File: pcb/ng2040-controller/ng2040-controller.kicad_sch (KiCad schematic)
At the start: 12 parts, among them J1 A, J2 B, J3 C, J4 D, J5 START, J6 SELECT, J7 JOY, J8 BATTERY, SW1 SW_DIP_x02, U1 RP2040-Zero, U2 NRF24L01_Breakout

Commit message: controller board
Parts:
- SW1: value SW_DIP_x02 -> OPTS
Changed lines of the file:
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@@
 			)
 		)
-		(property "Value" "SW_DIP_x02"
+		(property "Value" "OPTS"
 			(at 113.03 22.86 0)
 			(effects

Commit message: NG2040 controller board
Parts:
- U2: value NRF24L01_Breakout -> NRF24L01
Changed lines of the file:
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@@
 			)
 		)
-		(property "Value" "NRF24L01_Breakout"
+		(property "Value" "NRF24L01"
 			(at 176.53 66.0399 0)
 			(effects

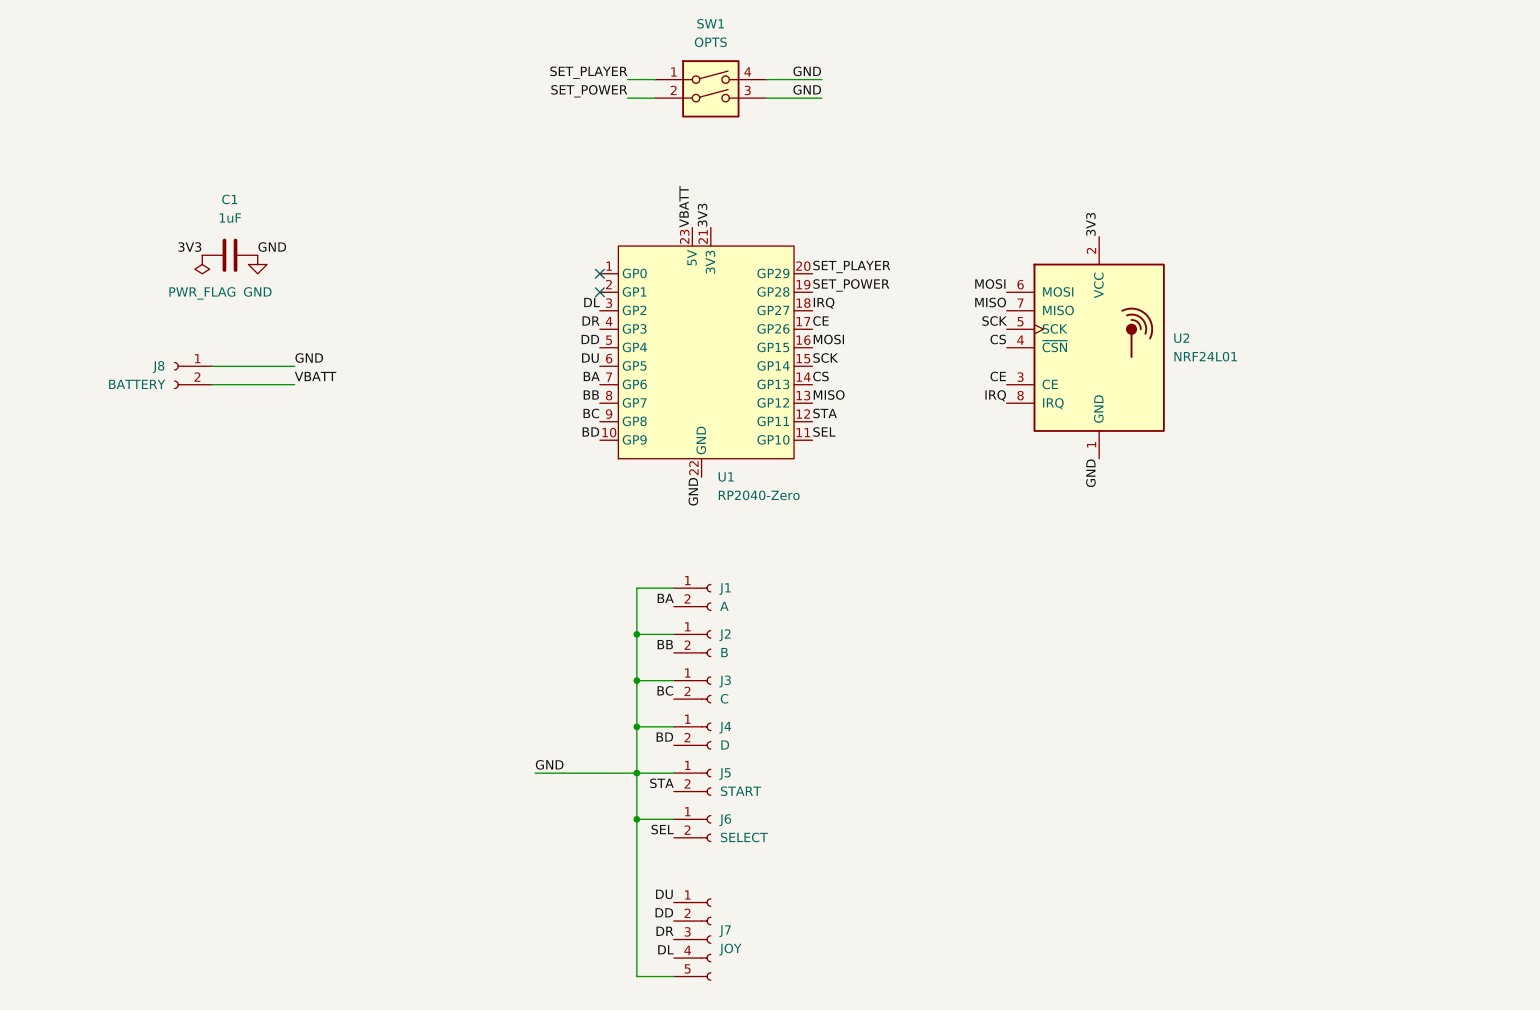
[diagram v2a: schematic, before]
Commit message: Reworking controller board to put pico on back for LED to shine through
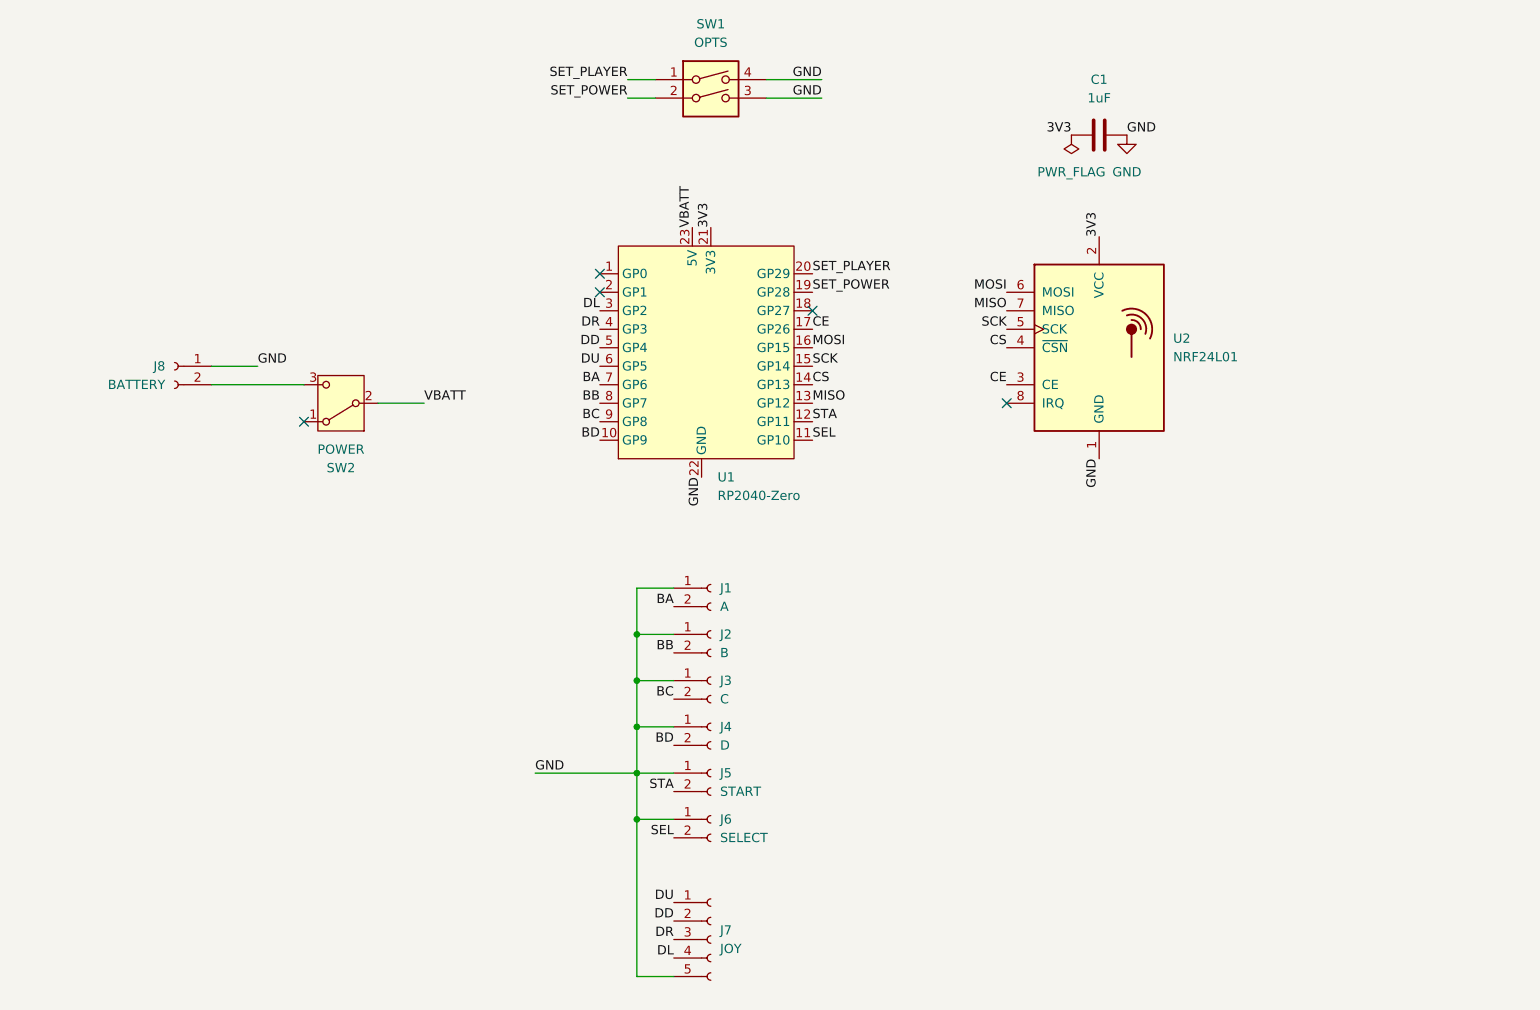
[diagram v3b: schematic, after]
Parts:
- added SW2: POWER, REB_Switch:REB_SlideSwitch_3pin, symbol Switch:SW_SPDT
- SW1: footprint Button_Switch_THT:SW_DIP_SPSTx02_Slide_9.78x7.26mm_W7.62mm_P2.54mm -> Button_Switch_SMD:SW_DIP_SPSTx02_Slide_6.7x6.64mm_W8.61mm_P2.54mm_LowProfile
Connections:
- net VBATT: now also SW2.2 (B); no longer J8.2 (Pin_2)
- net IRQ: no longer names the net of U2.8 (IRQ)
- net IRQ: no longer U1.18 (GP27)
- new net: J8.2 (Pin_2), SW2.3 (C)
- no-connect marks 2 -> 5
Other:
- moved on the sheet: C1
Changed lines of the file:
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@@
+	)
+	(no_connect
+		(at 153.67 72.39)
+	)
+	(no_connect
+		(at 57.15 74.93)
 	)
 	(no_connect
@@
 	)
 	(no_connect
+		(at 127 59.69)
+	)
+	(no_connect
 		(at 97.79 57.15)
 	)
@@
 	(wire
 		(pts
+			(xy 73.66 72.39) (xy 67.31 72.39)
+		)
+		(stroke
+			(width 0)
+			(type default)
+		)
+	)
+	(wire
+		(pts
 			(xy 102.87 97.79) (xy 102.87 104.14)
 		)
@@
 	(wire
 		(pts
-			(xy 55.88 67.31) (xy 44.45 67.31)
+			(xy 50.8 67.31) (xy 44.45 67.31)
 		)
 		(stroke
@@
 	(wire
 		(pts
-			(xy 55.88 69.85) (xy 44.45 69.85)
+			(xy 57.15 69.85) (xy 44.45 69.85)
 		)
 		(stroke
@@
 		)
 	)
-	(label "VBATT"
-		(at 55.88 69.85 0)
-		(fields_autoplaced yes)
-		(effects
-			(font
-				(size 1.27 1.27)
-			)
-			(justify left bottom)
-		)
-	)
 	(label "DL"
 		(at 97.79 59.69 180)
@@
 	)
 	(label "GND"
-		(at 55.88 67.31 0)
+		(at 50.8 67.31 0)
 		(fields_autoplaced yes)
 		(effects
@@
 		)
 	)
-	(label "IRQ"
-		(at 153.67 72.39 180)
-		(fields_autoplaced yes)
-		(effects
-			(font
-				(size 1.27 1.27)
-			)
-			(justify right bottom)
-		)
-	)
 	(label "3V3"
 		(at 166.37 49.53 90)
@@
 	)
 	(label "3V3"
-		(at 43.18 52.07 180)
+		(at 162.56 35.56 180)
 		(fields_autoplaced yes)
 		(effects
@@
 	)
 	(label "GND"
-		(at 50.8 52.07 0)
+		(at 170.18 35.56 0)
 		(fields_autoplaced yes)
 		(effects
@@
 		)
 	)
+	(label "VBATT"
+		(at 73.66 72.39 0)
+		(fields_autoplaced yes)
+		(effects
+			(font
+				(size 1.27 1.27)
+			)
+			(justify left bottom)
+		)
+	)
 	(label "MOSI"
 		(at 153.67 57.15 180)
@@
 			)
 			(justify right bottom)
-		)
-	)
-	(label "IRQ"
-		(at 127 59.69 0)
-		(fields_autoplaced yes)
-		(effects
-			(font
-				(size 1.27 1.27)
-			)
-			(justify left bottom)
 		)
 	)
@@
 				(path "/e91880d7-e1f1-43ba-b9bf-5f0fc90655d2"
 					(reference "J7")
+					(unit 1)
+				)
+			)
+		)
+	)
+	(symbol
+		(lib_id "Switch:SW_SPDT")
+		(at 62.23 72.39 180)
+		(unit 1)
+		(exclude_from_sim no)
+		(in_bom yes)
+		(on_board yes)
+		(dnp no)
+		(property "Reference" "SW2"
+			(at 62.23 81.28 0)
+			(effects
+				(font
+					(size 1.27 1.27)
+				)
+			)
+		)
+		(property "Value" "POWER"
+			(at 62.23 78.74 0)
+			(effects
+				(font
+					(size 1.27 1.27)
+				)
+			)
+		)
+		(property "Footprint" "REB_Switch:REB_SlideSwitch_3pin"
+			(at 62.23 72.39 0)
+			(effects
+				(font
+					(size 1.27 1.27)
+				)
+				(hide yes)
+			)
+		)
+		(property "Datasheet" "~"
+			(at 62.23 64.77 0)
+			(effects
+				(font
+					(size 1.27 1.27)
+				)
+				(hide yes)
+			)
+		)
+		(property "Description" "Switch, single pole double throw"
+			(at 62.23 72.39 0)
+			(effects
+				(font
+					(size 1.27 1.27)
+				)
+				(hide yes)
+			)
+		)
+		(property "Notes" ""
+			(at 62.23 72.39 0)
+			(effects
+				(font
+					(size 1.27 1.27)
+				)
+			)
+		)
+		(pin "2"
+		)
+		(pin "3"
+		)
+		(pin "1"
+		)
+		(instances
+			(project "ng2040-controller"
+				(path "/e91880d7-e1f1-43ba-b9bf-5f0fc90655d2"
+					(reference "SW2")
 					(unit 1)
 				)
@@
 			)
 		)
-		(property "Footprint" "Button_Switch_THT:SW_DIP_SPSTx02_Slide_9.78x7.26mm_W7.62mm_P2.54mm"
+		(property "Footprint" "Button_Switch_SMD:SW_DIP_SPSTx02_Slide_6.7x6.64mm_W8.61mm_P2.54mm_LowProfile"
 			(at 113.03 30.48 0)
 			(effects
@@
 	(symbol
 		(lib_id "power:PWR_FLAG")
-		(at 43.18 52.07 180)
+		(at 162.56 35.56 180)
 		(unit 1)
 		(exclude_from_sim no)
@@
 		(fields_autoplaced yes)
 		(property "Reference" "#FLG01"
-			(at 43.18 53.975 0)
+			(at 162.56 37.465 0)
 			(effects
 				(font
@@
 		)
 		(property "Value" "PWR_FLAG"
-			(at 43.18 57.15 0)
+			(at 162.56 40.64 0)
 			(effects
 				(font
@@
 		)
 		(property "Footprint" ""
-			(at 43.18 52.07 0)
+			(at 162.56 35.56 0)
 			(effects
 				(font
@@
 		)
 		(property "Datasheet" "~"
-			(at 43.18 52.07 0)
+			(at 162.56 35.56 0)
 			(effects
 				(font
@@
 		)
 		(property "Description" ""
-			(at 43.18 52.07 0)
+			(at 162.56 35.56 0)
 			(effects
 				(font
@@
 	(symbol
 		(lib_id "power:GND")
-		(at 50.8 52.07 0)
+		(at 170.18 35.56 0)
 		(unit 1)
 		(exclude_from_sim no)
@@
 		(fields_autoplaced yes)
 		(property "Reference" "#PWR01"
-			(at 50.8 58.42 0)
+			(at 170.18 41.91 0)
 			(effects
 				(font
@@
 		)
 		(property "Value" "GND"
-			(at 50.8 57.15 0)
+			(at 170.18 40.64 0)
 			(effects
 				(font
@@
 		)
 		(property "Footprint" ""
-			(at 50.8 52.07 0)
+			(at 170.18 35.56 0)
 			(effects
 				(font
@@
 		)
 		(property "Datasheet" ""
-			(at 50.8 52.07 0)
+			(at 170.18 35.56 0)
 			(effects
 				(font
@@
 		)
 		(property "Description" ""
-			(at 50.8 52.07 0)
+			(at 170.18 35.56 0)
 			(effects
 				(font
@@
 	(symbol
 		(lib_id "Device:C")
-		(at 46.99 52.07 90)
+		(at 166.37 35.56 90)
 		(unit 1)
 		(exclude_from_sim no)
@@
 		(fields_autoplaced yes)
 		(property "Reference" "C1"
-			(at 46.99 44.45 90)
+			(at 166.37 27.94 90)
 			(effects
 				(font
@@
 		)
 		(property "Value" "1uF"
-			(at 46.99 46.99 90)
+			(at 166.37 30.48 90)
 			(effects
 				(font
@@
 		)
 		(property "Footprint" "Capacitor_SMD:C_0805_2012Metric_Pad1.18x1.45mm_HandSolder"
-			(at 50.8 51.1048 0)
+			(at 170.18 34.5948 0)
 			(effects
 				(font
@@
 		)
 		(property "Datasheet" "~"
-			(at 46.99 52.07 0)
+			(at 166.37 35.56 0)
 			(effects
 				(font
@@
 		)
 		(property "Description" ""
-			(at 46.99 52.07 0)
-			(effects
-				(font
+			(at 166.37 35.56 0)
+			(effects
+				(font

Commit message: WIP changing controller into a narrower one breaking away NRF
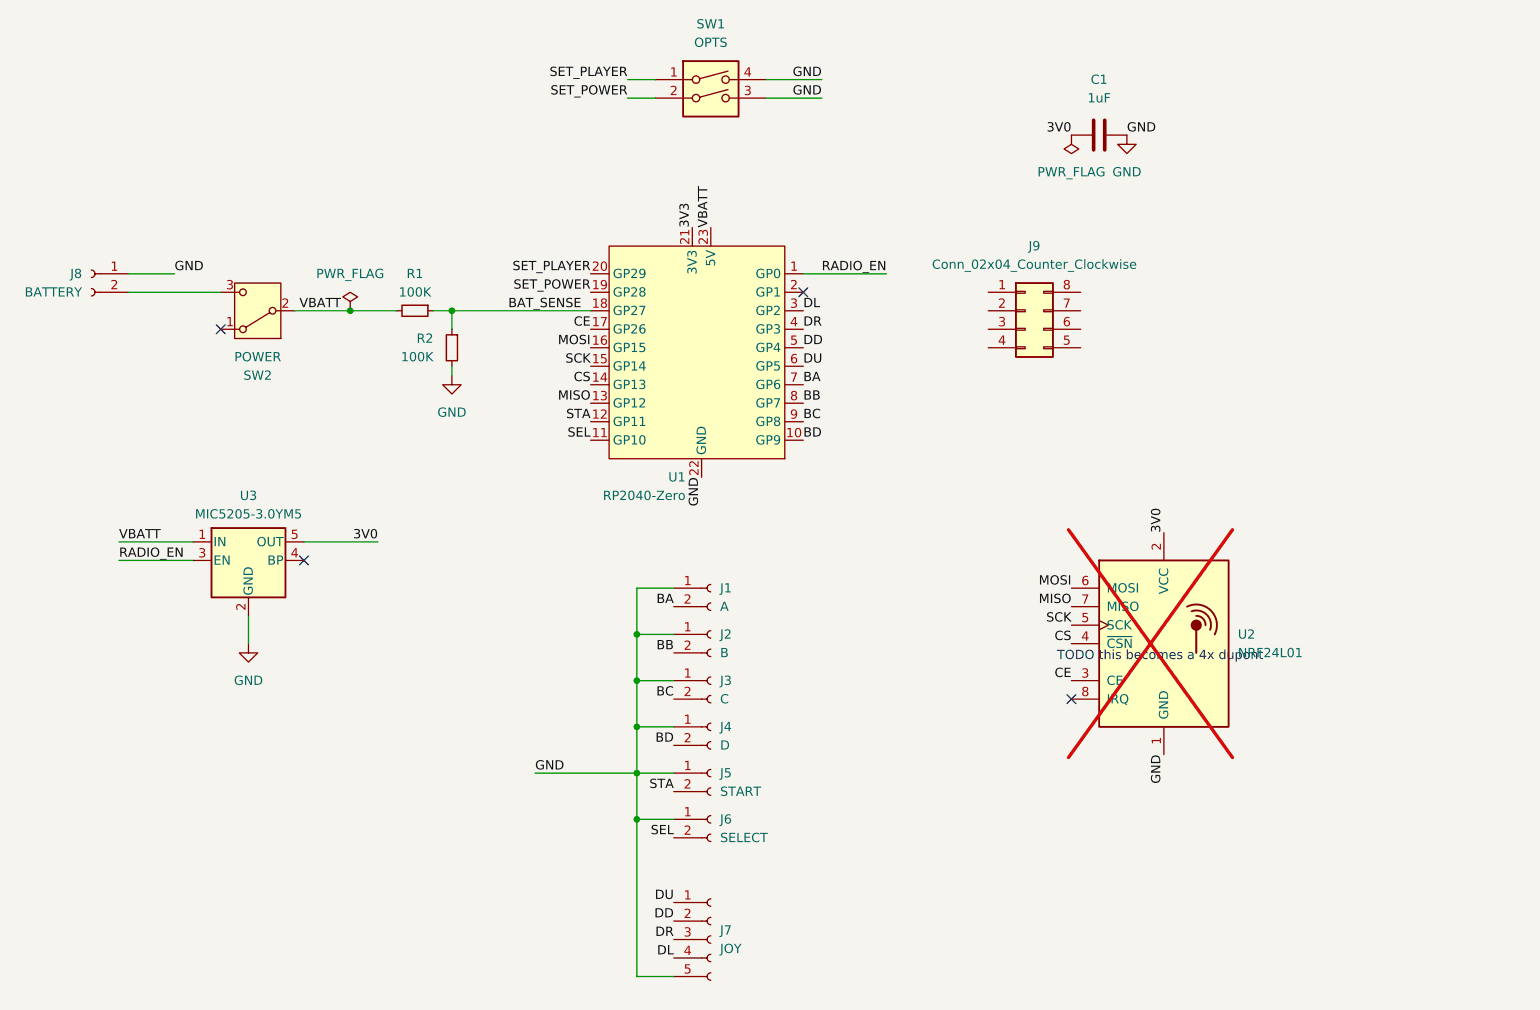
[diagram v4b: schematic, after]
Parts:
- added J9: Conn_02x04_Counter_Clockwise, Connector_PinHeader_2.54mm:PinHeader_2x04_P2.54mm_Vertical, symbol Connector_Generic:Conn_02x04_Counter_Clockwise
- added R1, R2: 100K, Resistor_SMD:R_0805_2012Metric_Pad1.20x1.40mm_HandSolder, symbol Device:R_Small
- added U3: MIC5205-3.0YM5, Package_TO_SOT_SMD:SOT-23-5, symbol Regulator_Linear:MIC5205-3.0YM5
- SW1: footprint Button_Switch_SMD:SW_DIP_SPSTx02_Slide_6.7x6.64mm_W8.61mm_P2.54mm_LowProfile -> Button_Switch_THT:SW_Slide_SPDT_Angled_CK_OS102011MA1Q
- U2: now not fitted
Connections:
- net 3V3: no longer C1.1, U2.2 (VCC)
- net GND: now also R2.2, U3.2 (GND)
- net VBATT: now also R1.2, U3.1 (IN)
- net RADIO_EN: now reaches U1.1 (GP0)
- net RADIO_EN: now also U3.3 (EN)
- net BAT_SENSE: now reaches U1.18 (GP27)
- net BAT_SENSE: now also R1.1, R2.1
- new net 3V0: C1.1, U2.2 (VCC), U3.5 (OUT)
- no-connect marks 5 -> 4
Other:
- note added: "TODO this becomes a 4x dupont"
- moved on the sheet: J8, SW2, U1

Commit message: Revise controller pcb, still use RP2040 but break out to radio daughterboard pointing up
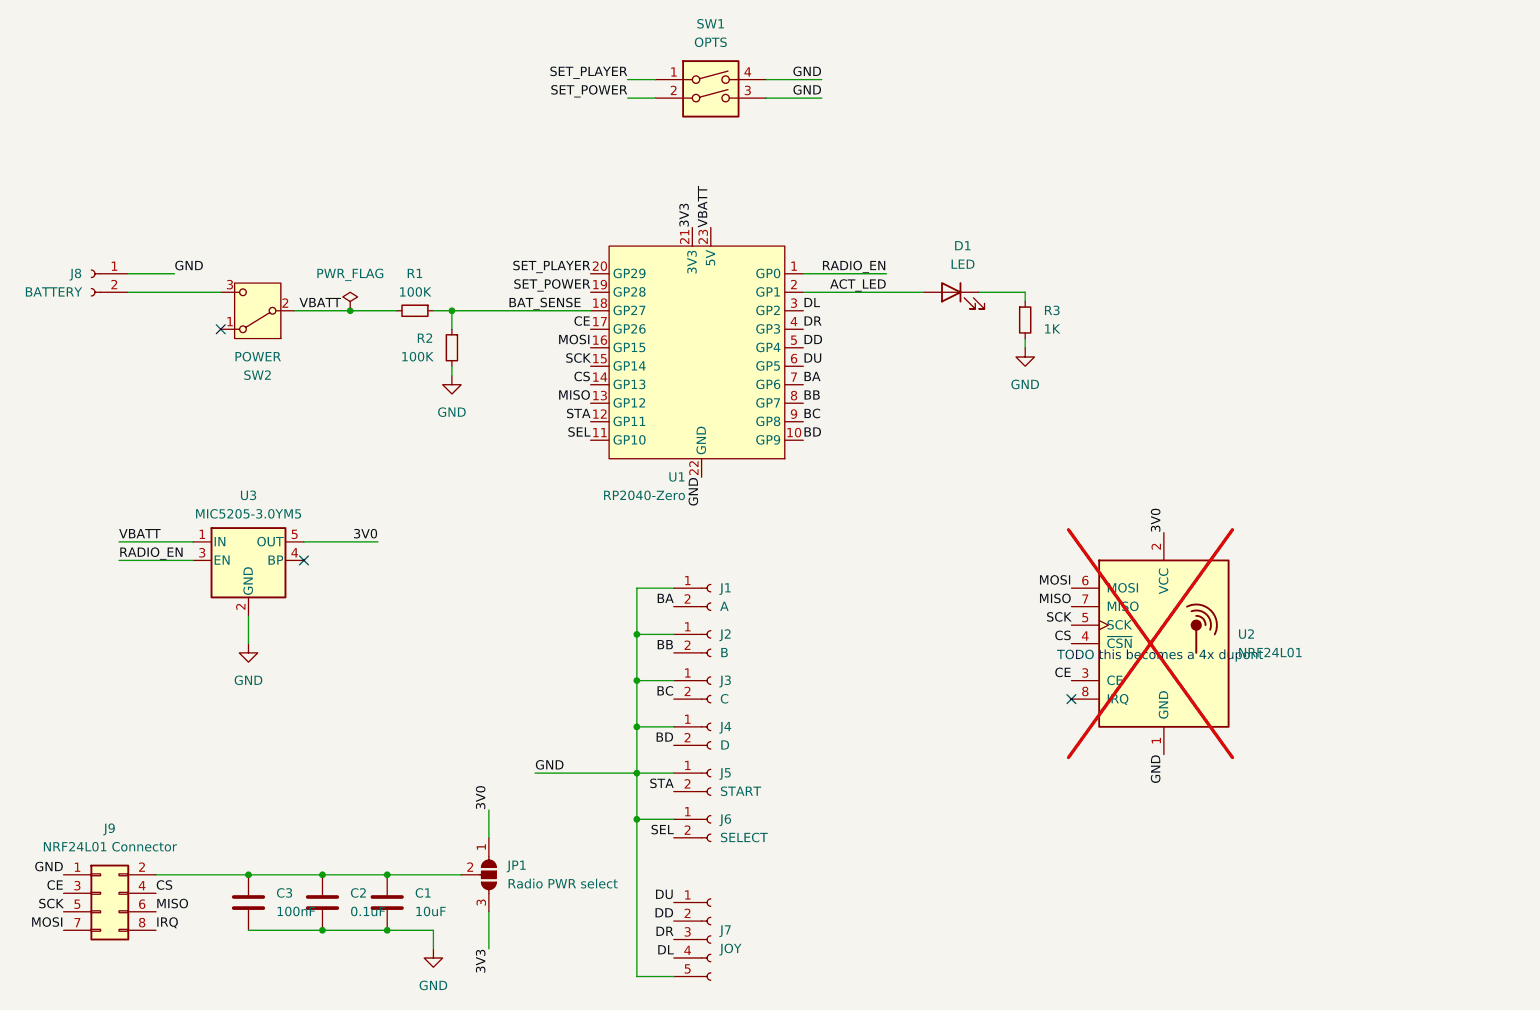
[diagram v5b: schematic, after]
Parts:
- added C2: 0.1uF, Capacitor_SMD:C_0805_2012Metric_Pad1.18x1.45mm_HandSolder, symbol Device:C
- added C3: 100nF, Capacitor_SMD:C_0805_2012Metric_Pad1.18x1.45mm_HandSolder, symbol Device:C
- added D1: LED, LED_THT:LED_D3.0mm_Horizontal_O1.27mm_Z6.0mm, symbol Device:LED
- added JP1: Radio PWR select, Jumper:SolderJumper-3_P1.3mm_Open_RoundedPad1.0x1.5mm, symbol Jumper:SolderJumper_3_Open
- added R3: 1K, Resistor_SMD:R_0805_2012Metric_Pad1.20x1.40mm_HandSolder, symbol Device:R_Small
- C1: value 1uF -> 10uF
- J9: value Conn_02x04_Counter_Clockwise -> NRF24L01 Connector; symbol Connector_Generic:Conn_02x04_Counter_Clockwise -> Connector_Generic:Conn_02x04_Odd_Even
- SW1: footprint Button_Switch_THT:SW_Slide_SPDT_Angled_CK_OS102011MA1Q -> Button_Switch_SMD:SW_DIP_SPSTx02_Slide_6.7x6.64mm_W8.61mm_P2.54mm_LowProfile
- SW2: footprint REB_Switch:REB_SlideSwitch_3pin -> Button_Switch_THT:SW_Slide_SPDT_Angled_CK_OS102011MA1Q
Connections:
- net 3V0: now also JP1.1 (A); no longer C1.1
- net 3V3: now also JP1.3 (B)
- net CE: now also J9.3 (Pin_3)
- net CS: now also J9.4 (Pin_4)
- net GND: now also C1.1, J9.1 (Pin_1), C2.1, C3.1, R3.2; no longer C1.2
- net MISO: now also J9.6 (Pin_6)
- net MOSI: now also J9.7 (Pin_7)
- net SCK: now also J9.5 (Pin_5)
- net at J9.2 (Pin_2): now also C1.2, C2.2, C3.2, JP1.2 (C)
- net IRQ: now reaches J9.8 (Pin_8)
- net ACT_LED: now reaches U1.2 (GP1)
- net ACT_LED: now also D1.2 (A)
- new net: D1.1 (K), R3.1
- no-connect marks 4 -> 3
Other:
- moved on the sheet: J9
